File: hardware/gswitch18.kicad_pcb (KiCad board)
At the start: 2 copper layers, 48.2 x 32 mm, 25 parts, among them IC1 ATMEGA88P, P1 CONN_6X2, P2 CONN_6X2, P3 CONN_6X2, P4 USB, P5 ISP, X1 12MHz

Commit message: v1.2 KiCAD 6 final changes
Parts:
- removed 1H6x4 (x3): P***, 1H6x4
- added C1: 0u1, Capacitor_SMD:C_0603_1608Metric, F.Cu at (115.2, 64.9)
- added MH1: P***, MountingHole:MountingHole_3.2mm_M3_Pad_Via, F.Cu at (79.6, 54.4)
- added MH2: P***, MountingHole:MountingHole_3.2mm_M3_Pad_Via, F.Cu at (120.6, 54.4)
- added MH4: P***, MountingHole:MountingHole_3.2mm_M3_Pad_Via, F.Cu at (120.7, 79.3)
- D3, D4: value 3.6v_Zen -> 3V6
- MH3: renamed from 1H6x4; footprint 1H6x4 -> MountingHole:MountingHole_3.2mm_M3_Pad_Via
- U1: renamed from IC1; footprint TQFP32 -> Package_QFP:TQFP-32_7x7mm_P0.8mm
- moved C2 0.81 mm to (115.2, 68.0)
- moved MH3 0.20 mm to (79.6, 79.1)
- turned D1 to -90 degrees
- turned D2 to -90 degrees
- renumbered C1 to C2, C2 to C5
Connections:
- D1 pad 1: GND -> Net-(D1-Pad1)
- D1 pad 2: N-000008 -> GND
- D2 pad 1: GND -> Net-(D2-Pad1)
- D2 pad 2: N-000029 -> GND
- D3 pad 2: N-000029 -> Net-(D2-Pad1)
- D4 pad 2: N-000008 -> Net-(D1-Pad1)
- MH3 pad : (no net) -> GND
- P4 pad 4: (no net) -> unconnected-(P4-Pad4)
- R1 pad 1: N-000008 -> Net-(D1-Pad1)
- R2 pad 1: N-000029 -> Net-(D2-Pad1)
- R3 pad 2: N-000029 -> Net-(D2-Pad1)
- R5 pad 2: N-000008 -> Net-(D1-Pad1)
- R6 pad 2: N-000029 -> Net-(D2-Pad1)
- U1 pad 19: (no net) -> unconnected-(U1-Pad19)
- U1 pad 20: (no net) -> unconnected-(U1-Pad20)
- U1 pad 22: (no net) -> unconnected-(U1-Pad22)
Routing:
- net Net-(D1-Pad1): track 0.00 -> 13.8 mm, vias 0 -> 2
- net N-000008: track 13.7 -> 0.00 mm, vias 2 -> 0
- net Net-(D2-Pad1): track 0.00 -> 13.3 mm
- net N-000029: track 13.3 -> 0.00 mm
- net GND: track 3.36 -> 9.99 mm, vias 28 -> 24
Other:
- board text added: "v1.2"
- board text removed: "gSwitch18 v1.2"

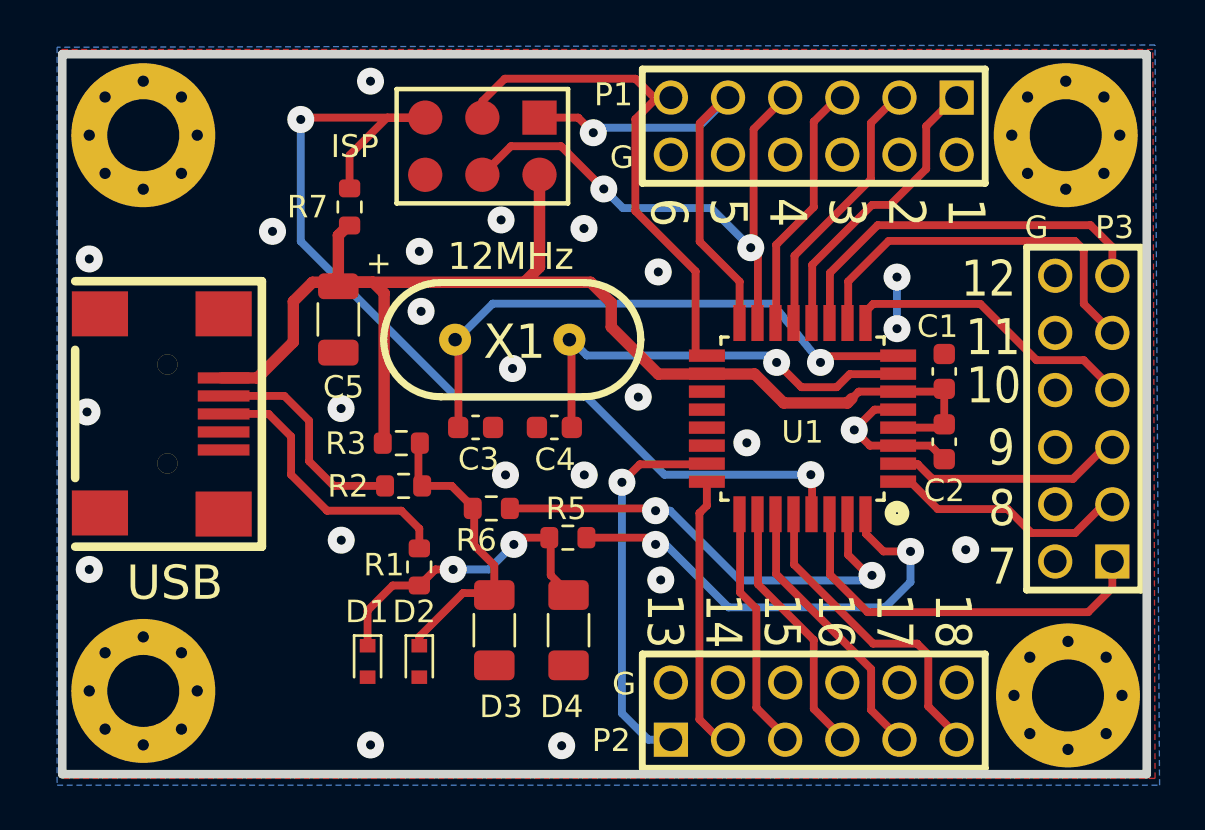
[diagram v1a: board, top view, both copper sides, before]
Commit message: Updated to KiCAD v6. Bumped versionto v1.2 TH (through-hole). DEPRECATED; See smd branch.
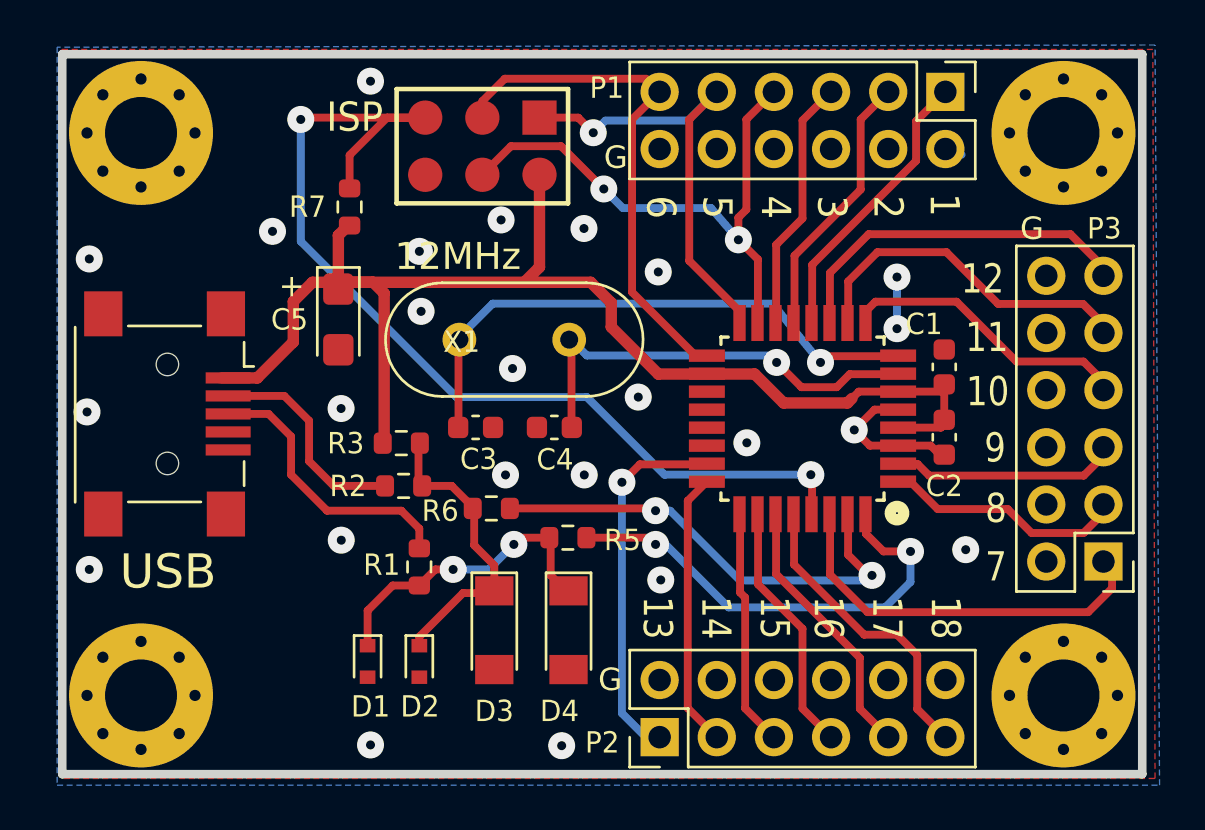
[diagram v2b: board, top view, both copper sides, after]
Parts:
- C5: footprint Capacitor_SMD:C_1206_3216Metric -> Capacitor_Tantalum_SMD:CP_EIA-3216-18_Kemet-A
- D3, D4: footprint Capacitor_SMD:C_1206_3216Metric_Pad1.33x1.80mm_HandSolder -> Diode_SMD:D_MiniMELF
- MH1, MH2, MH3, MH4: value P*** -> 3.2mm
- P1, P2, P3: footprint pin_array_6x2 -> Connector_PinHeader_2.54mm:PinHeader_2x06_P2.54mm_Vertical
- P4: footprint USB-B_mini -> Connector_USB:USB_Mini-B_Lumberg_2486_01_Horizontal
- X1: footprint HC-49V -> Crystal:Crystal_HC49-4H_Vertical
- moved P2 6.95 mm to (102.5, 81.2), turned to 90 degrees
- moved P3 6.41 mm to (122.3, 73.3), turned to 180 degrees
- moved P1 6.04 mm to (115.2, 52.5), turned to -90 degrees
- moved X1 2.35 mm to (93.7, 63.5)
- moved MH3 0.22 mm to (79.5, 79.3)
- moved C1 0.20 mm to (115.2, 64.7)
- moved C2 0.20 mm to (115.2, 67.8)
- moved MH4 0.20 mm to (120.5, 79.3)
- moved MH1 0.14 mm to (79.5, 54.3)
- moved MH2 0.14 mm to (120.5, 54.3)
- turned D3 to -90 degrees
- turned D4 to -90 degrees
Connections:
- D1 pad 1: Net-(D1-Pad1) -> Net-(D4-Pad1)
- D2 pad 1: Net-(D2-Pad1) -> Net-(D3-Pad1)
- D3 pad 1: GND -> Net-(D3-Pad1)
- D3 pad 2: Net-(D2-Pad1) -> GND
- D4 pad 1: GND -> Net-(D4-Pad1)
- D4 pad 2: Net-(D1-Pad1) -> GND
- R1 pad 1: Net-(D1-Pad1) -> Net-(D4-Pad1)
- R2 pad 1: Net-(D2-Pad1) -> Net-(D3-Pad1)
- R3 pad 2: Net-(D2-Pad1) -> Net-(D3-Pad1)
- R5 pad 2: Net-(D1-Pad1) -> Net-(D4-Pad1)
- R6 pad 2: Net-(D2-Pad1) -> Net-(D3-Pad1)
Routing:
- net Net-(D4-Pad1): track 0.00 -> 13.8 mm, vias 0 -> 2
- net Net-(D1-Pad1): track 13.8 -> 0.00 mm, vias 2 -> 0
- net Net-(D3-Pad1): track 0.00 -> 13.3 mm
- net Net-(D2-Pad1): track 13.3 -> 0.00 mm
- net /SCK: track 23.9 -> 21.8 mm
- net /SW11: track 16.9 -> 15.1 mm
- net /SW12: track 16.8 -> 15.7 mm
- net /SW18: track 13.6 -> 13.0 mm
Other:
- board size 48.2 x 32 mm -> 48 x 32 mm
- board text added: "1"
- board text added: "2"
- board text added: "3"
- board text added: "4"
- board text added: "5"
- board text added: "6"
- board text removed: "1 2 3 4 5 6"
